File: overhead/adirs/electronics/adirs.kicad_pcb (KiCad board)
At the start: 2 copper layers, 3 parts

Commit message: Exported DSN and SES for ADIRS
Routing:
- net Net-(KR1-+5V_TOP_LED): track 0.00 -> 18.6 mm
- net Net-(KR1-GND_TOP_LED): track 0.06 -> 16.5 mm
- net Net-(KR1-+5V_BOTTOM_LED): track 0.00 -> 2.54 mm
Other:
- board outline added: 147.7 x 51.2 mm
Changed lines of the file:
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@@
 		(layer "Dwgs.User")
 	)
+	(gr_rect
+		(start 47.2 97.4)
+		(end 194.9 148.6)
+		(stroke
+			(width 0.05)
+			(type default)
+		)
+		(fill no)
+		(layer "Edge.Cuts")
+	)
 	(segment
-		(start 96.65 125.79)
-		(end 96.61 125.75)
+		(start 97.9617 123.79)
+		(end 96.0017 125.75)
 		(width 0.2)
 		(layer "F.Cu")
 		(net 1)
 	)
+	(segment
+		(start 94.95 125.75)
+		(end 96.0017 125.75)
+		(width 0.2)
+		(layer "F.Cu")
+		(net 1)
+	)
+	(segment
+		(start 110.65 123.79)
+		(end 97.9617 123.79)
+		(width 0.2)
+		(layer "F.Cu")
+		(net 1)
+	)
+	(segment
+		(start 110.65 126.33)
+		(end 110.65 128.87)
+		(width 0.2)
+		(layer "B.Cu")
+		(net 2)
+	)
+	(segment
+		(start 102.5583 128.29)
+		(end 109.5983 121.25)
+		(width 0.2)
+		(layer "B.Cu")
+		(net 3)
+	)
+	(segment
+		(start 110.65 121.25)
+		(end 109.5983 121.25)
+		(width 0.2)
+		(layer "B.Cu")
+		(net 3)
+	)
+	(segment
+		(start 94.95 128.29)
+		(end 102.5583 128.29)
+		(width 0.2)
+		(layer "B.Cu")
+		(net 3)
+	)
 	(embedded_fonts no)

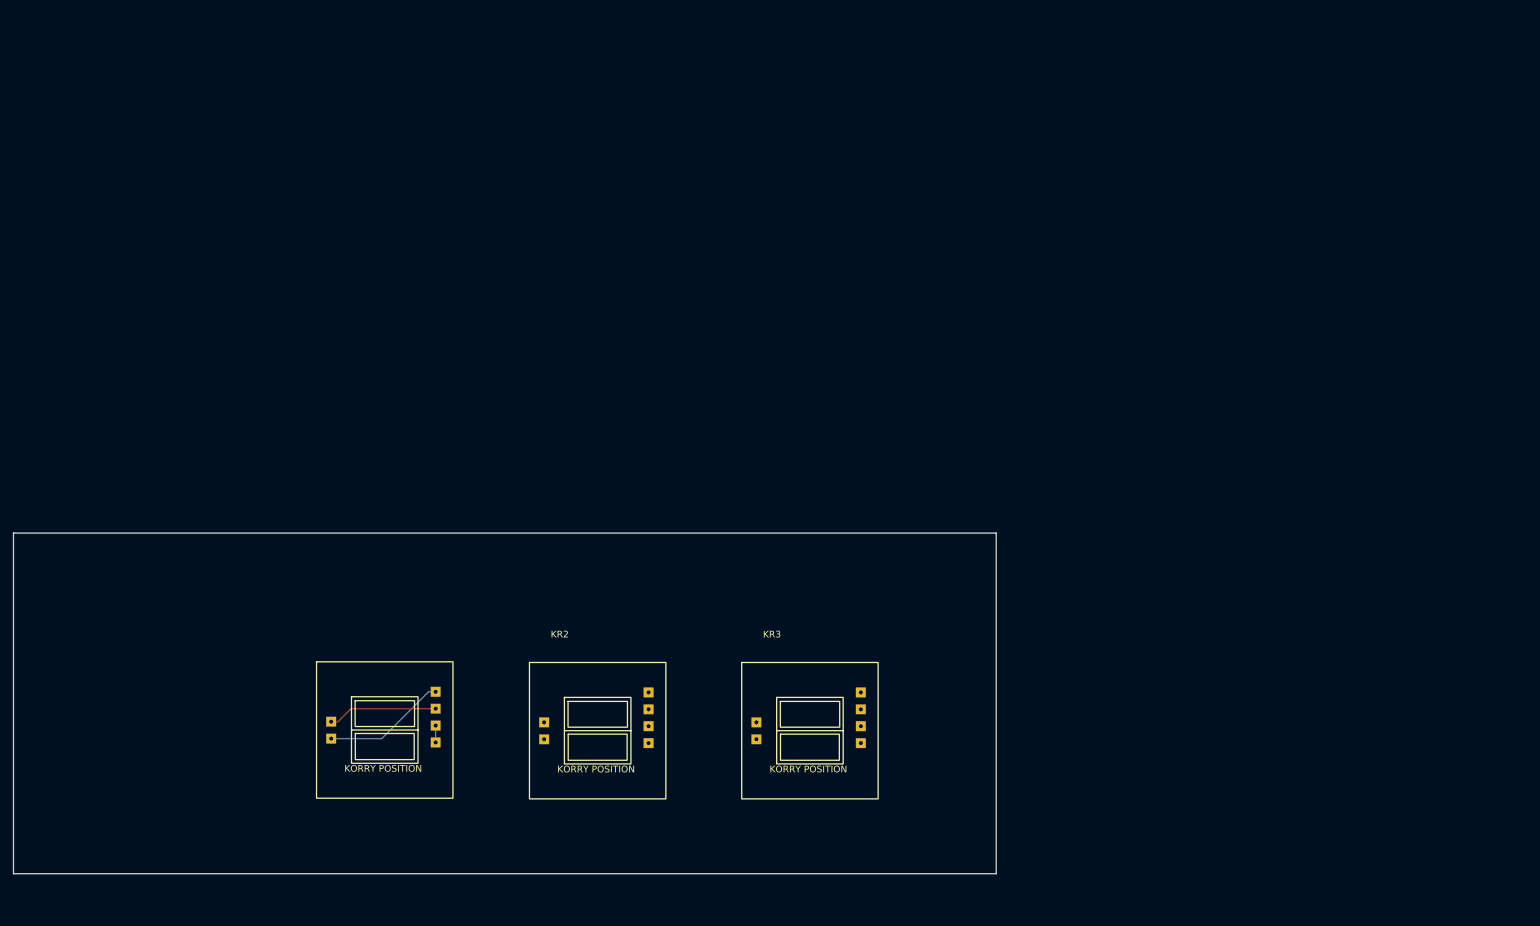
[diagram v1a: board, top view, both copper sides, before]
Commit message: Started work for ADIRS Schematic and PCB
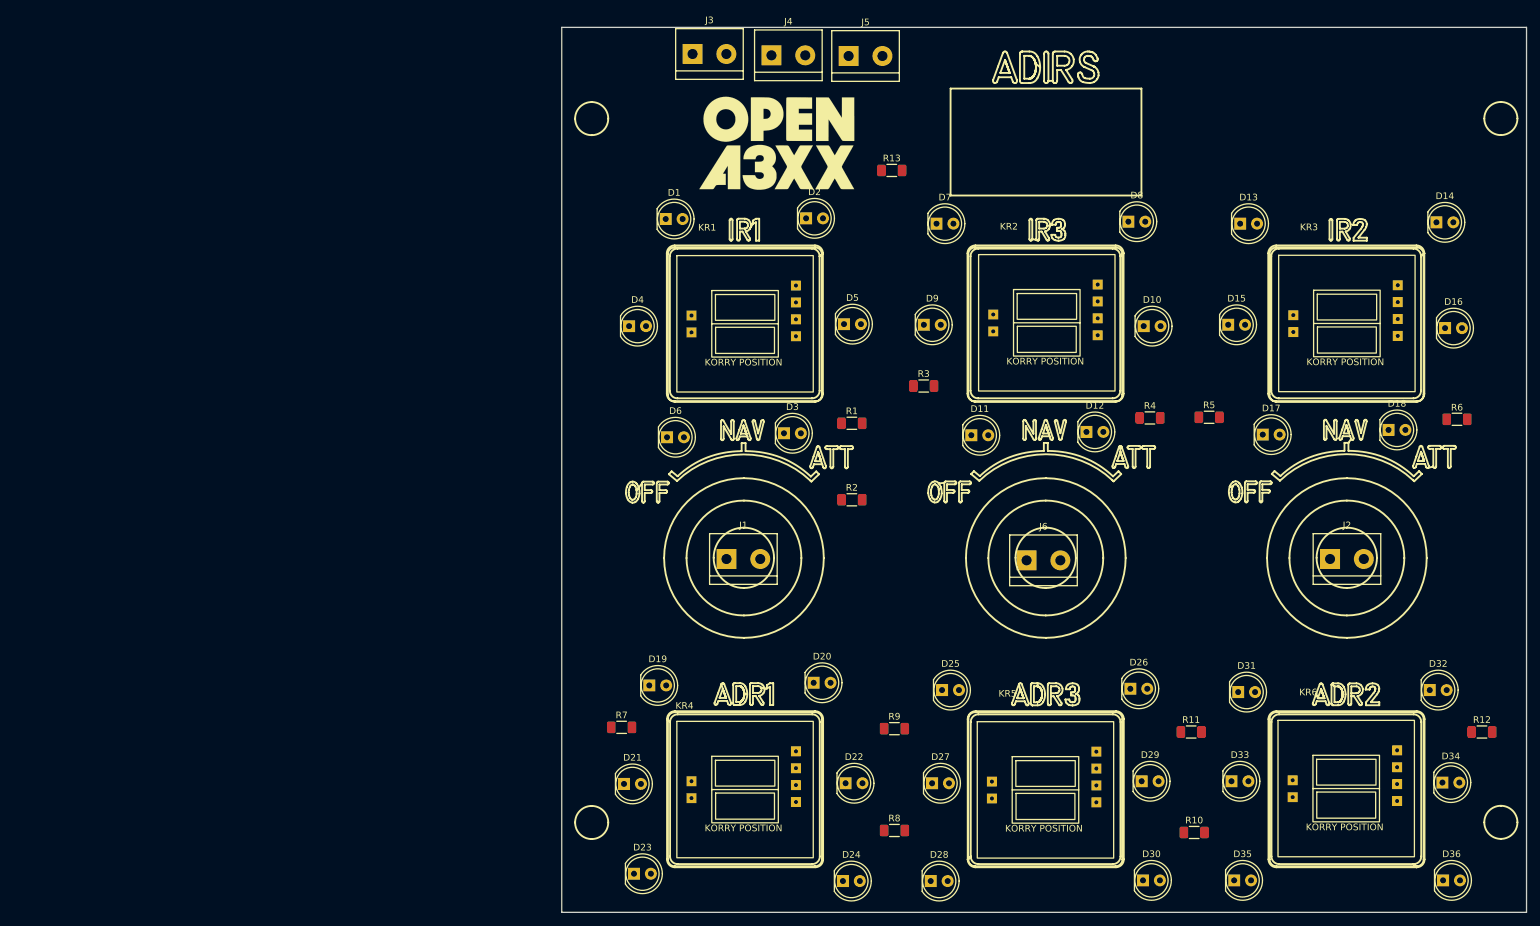
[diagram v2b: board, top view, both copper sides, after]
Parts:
- added D1: LED, LED_THT:LED_D5.0mm, F.Cu at (145.2, 50.2)
- added D10: LED, LED_THT:LED_D5.0mm, F.Cu at (217.1, 66.3)
- added D11: LED, LED_THT:LED_D5.0mm, F.Cu at (191.2, 82.7)
- added D12: LED, LED_THT:LED_D5.0mm, F.Cu at (208.5, 82.2)
- added D13: LED, LED_THT:LED_D5.0mm, F.Cu at (231.6, 50.9)
- added D14: LED, LED_THT:LED_D5.0mm, F.Cu at (261.1, 50.7)
- added D15: LED, LED_THT:LED_D5.0mm, F.Cu at (229.8, 66.1)
- added D16: LED, LED_THT:LED_D5.0mm, F.Cu at (262.4, 66.6)
- added D17: LED, LED_THT:LED_D5.0mm, F.Cu at (235.0, 82.6)
- added D18: LED, LED_THT:LED_D5.0mm, F.Cu at (253.9, 81.9)
- added D19: LED, LED_THT:LED_D5.0mm, F.Cu at (142.8, 120.3)
- added D2: LED, LED_THT:LED_D5.0mm, F.Cu at (166.3, 50.1)
- added D20: LED, LED_THT:LED_D5.0mm, F.Cu at (167.5, 119.9)
- added D21: LED, LED_THT:LED_D5.0mm, F.Cu at (139.0, 135.1)
- added D22: LED, LED_THT:LED_D5.0mm, F.Cu at (172.3, 135.0)
- added D23: LED, LED_THT:LED_D5.0mm, F.Cu at (140.5, 148.6)
- added D24: LED, LED_THT:LED_D5.0mm, F.Cu at (171.9, 149.7)
- added D25: LED, LED_THT:LED_D5.0mm, F.Cu at (186.8, 121.0)
- added D26: LED, LED_THT:LED_D5.0mm, F.Cu at (215.1, 120.8)
- added D27: LED, LED_THT:LED_D5.0mm, F.Cu at (185.3, 135.0)
- added D28: LED, LED_THT:LED_D5.0mm, F.Cu at (185.1, 149.7)
- added D29: LED, LED_THT:LED_D5.0mm, F.Cu at (216.8, 134.7)
- added D3: LED, LED_THT:LED_D5.0mm, F.Cu at (163.0, 82.4)
- added D30: LED, LED_THT:LED_D5.0mm, F.Cu at (217.0, 149.6)
- added D31: LED, LED_THT:LED_D5.0mm, F.Cu at (231.3, 121.3)
- added D32: LED, LED_THT:LED_D5.0mm, F.Cu at (260.1, 121.0)
- added D33: LED, LED_THT:LED_D5.0mm, F.Cu at (230.3, 134.7)
- added D34: LED, LED_THT:LED_D5.0mm, F.Cu at (262.0, 134.9)
- added D35: LED, LED_THT:LED_D5.0mm, F.Cu at (230.7, 149.6)
- added D36: LED, LED_THT:LED_D5.0mm, F.Cu at (262.1, 149.6)
- added D4: LED, LED_THT:LED_D5.0mm, F.Cu at (139.7, 66.3)
- added D5: LED, LED_THT:LED_D5.0mm, F.Cu at (172.0, 66.0)
- added D6: LED, LED_THT:LED_D5.0mm, F.Cu at (145.4, 83.0)
- added D7: LED, LED_THT:LED_D5.0mm, F.Cu at (185.9, 50.9)
- added D8: LED, LED_THT:LED_D5.0mm, F.Cu at (214.8, 50.6)
- added D9: LED, LED_THT:LED_D5.0mm, F.Cu at (184.0, 66.1)
- added G***: LOGO, opena3x:Logo, F.Cu at (161.5, 39.0)
- added J1: Conn_02x01, TerminalBlock:TerminalBlock_bornier-2_P5.08mm, F.Cu at (154.4, 101.3)
- added J2: Conn_02x13_Counter_Clockwise, TerminalBlock:TerminalBlock_bornier-2_P5.08mm, F.Cu at (245.1, 101.3)
- added J3: Conn_02x01, TerminalBlock:TerminalBlock_bornier-2_P5.08mm, F.Cu at (149.3, 25.4)
- added J4: Conn_02x02_Counter_Clockwise, TerminalBlock:TerminalBlock_bornier-2_P5.08mm, F.Cu at (161.1, 25.6)
- added J5: Conn_02x02_Counter_Clockwise, TerminalBlock:TerminalBlock_bornier-2_P5.08mm, F.Cu at (172.7, 25.7)
- added J6: Conn_02x02_Counter_Clockwise, TerminalBlock:TerminalBlock_bornier-2_P5.08mm, F.Cu at (199.5, 101.5)
- added KR4: ~, KorrySwitch:OpenA3XX, F.Cu at (146.9, 125.7)
- added KR5: ~, KorrySwitch:OpenA3XX, F.Cu at (192.1, 125.8)
- added KR6: ~, KorrySwitch:OpenA3XX, F.Cu at (237.2, 125.5)
- added R1: 220R, Resistor_SMD:R_1206_3216Metric_Pad1.30x1.75mm_HandSolder, F.Cu at (173.2, 80.9)
- added R10: 220R, Resistor_SMD:R_1206_3216Metric_Pad1.30x1.75mm_HandSolder, F.Cu at (224.7, 142.4)
- added R11: 220R, Resistor_SMD:R_1206_3216Metric_Pad1.30x1.75mm_HandSolder, F.Cu at (224.2, 127.3)
- added R12: 220R, Resistor_SMD:R_1206_3216Metric_Pad1.30x1.75mm_HandSolder, F.Cu at (267.9, 127.3)
- added R13: 220R, Resistor_SMD:R_1206_3216Metric_Pad1.30x1.75mm_HandSolder, F.Cu at (179.2, 42.9)
- added R2: 220R, Resistor_SMD:R_1206_3216Metric_Pad1.30x1.75mm_HandSolder, F.Cu at (173.2, 92.4)
- added R3: 220R, Resistor_SMD:R_1206_3216Metric_Pad1.30x1.75mm_HandSolder, F.Cu at (184.0, 75.3)
- added R4: 220R, Resistor_SMD:R_1206_3216Metric_Pad1.30x1.75mm_HandSolder, F.Cu at (218.0, 80.1)
- added R5: 220R, Resistor_SMD:R_1206_3216Metric_Pad1.30x1.75mm_HandSolder, F.Cu at (226.9, 80.0)
- added R6: 220R, Resistor_SMD:R_1206_3216Metric_Pad1.30x1.75mm_HandSolder, F.Cu at (264.1, 80.3)
- added R7: 220R, Resistor_SMD:R_1206_3216Metric_Pad1.30x1.75mm_HandSolder, F.Cu at (138.6, 126.6)
- added R8: 220R, Resistor_SMD:R_1206_3216Metric_Pad1.30x1.75mm_HandSolder, F.Cu at (179.6, 142.1)
- added R9: 220R, Resistor_SMD:R_1206_3216Metric_Pad1.30x1.75mm_HandSolder, F.Cu at (179.6, 126.8)
- moved KR3 101.3 mm to (237.3, 55.6)
- moved KR2 91.2 mm to (192.2, 55.5)
- moved KR1 81.6 mm to (146.9, 55.7)
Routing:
- net Net-(KR1-+5V_TOP_LED): track 18.6 -> 0.00 mm
- net Net-(KR1-GND_TOP_LED): track 16.5 -> 0.00 mm
- net Net-(KR1-+5V_BOTTOM_LED): track 2.54 -> 0.00 mm
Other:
- board size 147.7 x 51.2 mm -> 145 x 133 mm

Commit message: Updates and Routing to ADIRS PCB and Schematic
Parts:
- removed the G*** at (161.5, 39.0)
- added D37: LED, LED_THT:LED_D5.0mm, F.Cu at (188.4, 27.2)
- added D38: LED, LED_THT:LED_D5.0mm, F.Cu at (182.1, 37.8)
- added D39: LED, LED_THT:LED_D5.0mm, F.Cu at (213.3, 27.4)
- added D40: LED, LED_THT:LED_D5.0mm, F.Cu at (218.4, 39.1)
- added G***: LOGO, opena3x:Logo, F.Cu at (162.4, 39.8)
- added G***: LOGO, opena3x:Logo, B.Cu at (164.3, 39.2)
- added R14: 220R, Resistor_SMD:R_1206_3216Metric_Pad1.30x1.75mm_HandSolder, F.Cu at (224.6, 30.6)
- added R15: 220R, Resistor_SMD:R_1206_3216Metric_Pad1.30x1.75mm_HandSolder, F.Cu at (228.6, 39.3)
- J2: footprint TerminalBlock:TerminalBlock_bornier-2_P5.08mm -> Connector_PinHeader_2.54mm:PinHeader_2x14_P2.54mm_Vertical; moved to B.Cu
- J3: footprint TerminalBlock:TerminalBlock_bornier-2_P5.08mm -> Connector_PinHeader_2.54mm:PinHeader_1x02_P2.54mm_Vertical
- J4, J5, J6: footprint TerminalBlock:TerminalBlock_bornier-2_P5.08mm -> TerminalBlock:TerminalBlock_bornier-4_P5.08mm
- moved J5 111.8 mm to (255.2, 101.2), turned to 180 degrees
- moved J2 76.5 mm to (235.1, 25.5), turned to -90 degrees
- moved J1 76.0 mm to (154.2, 25.3), turned to 180 degrees
- moved J4 75.6 mm to (164.6, 101.1), turned to 180 degrees
- moved J3 56.7 mm to (204.4, 38.5), turned to -90 degrees
- moved J6 10.4 mm to (209.9, 101.1), turned to 180 degrees
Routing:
- net GND: track 0.00 -> 680.1 mm, vias 0 -> 4
- net +12V: track 0.00 -> 470.3 mm, vias 0 -> 3
- net Net-(J2-Pin_15): track 0.00 -> 208.4 mm, vias 0 -> 1
- net Net-(J2-Pin_14): track 0.00 -> 191.0 mm, vias 0 -> 1
- net Net-(J2-Pin_13): track 0.00 -> 185.4 mm, vias 0 -> 1
- net Net-(J2-Pin_21): track 0.00 -> 178.1 mm, vias 0 -> 1
- net Net-(J2-Pin_22): track 0.00 -> 177.3 mm, vias 0 -> 1
- net Net-(J2-Pin_20): track 0.00 -> 161.9 mm, vias 0 -> 2
- net Net-(J2-Pin_9): track 0.00 -> 146.7 mm, vias 0 -> 1
- net Net-(J2-Pin_28): track 0.00 -> 145.5 mm, vias 0 -> 1
- net Net-(J2-Pin_27): track 0.00 -> 143.3 mm, vias 0 -> 1
- net Net-(J2-Pin_7): track 0.00 -> 133.6 mm, vias 0 -> 2
- net Net-(J2-Pin_26): track 0.00 -> 132.6 mm, vias 0 -> 1
- net Net-(J2-Pin_3): track 0.00 -> 128.6 mm, vias 0 -> 1
- net Net-(J2-Pin_8): track 0.00 -> 125.0 mm, vias 0 -> 1
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
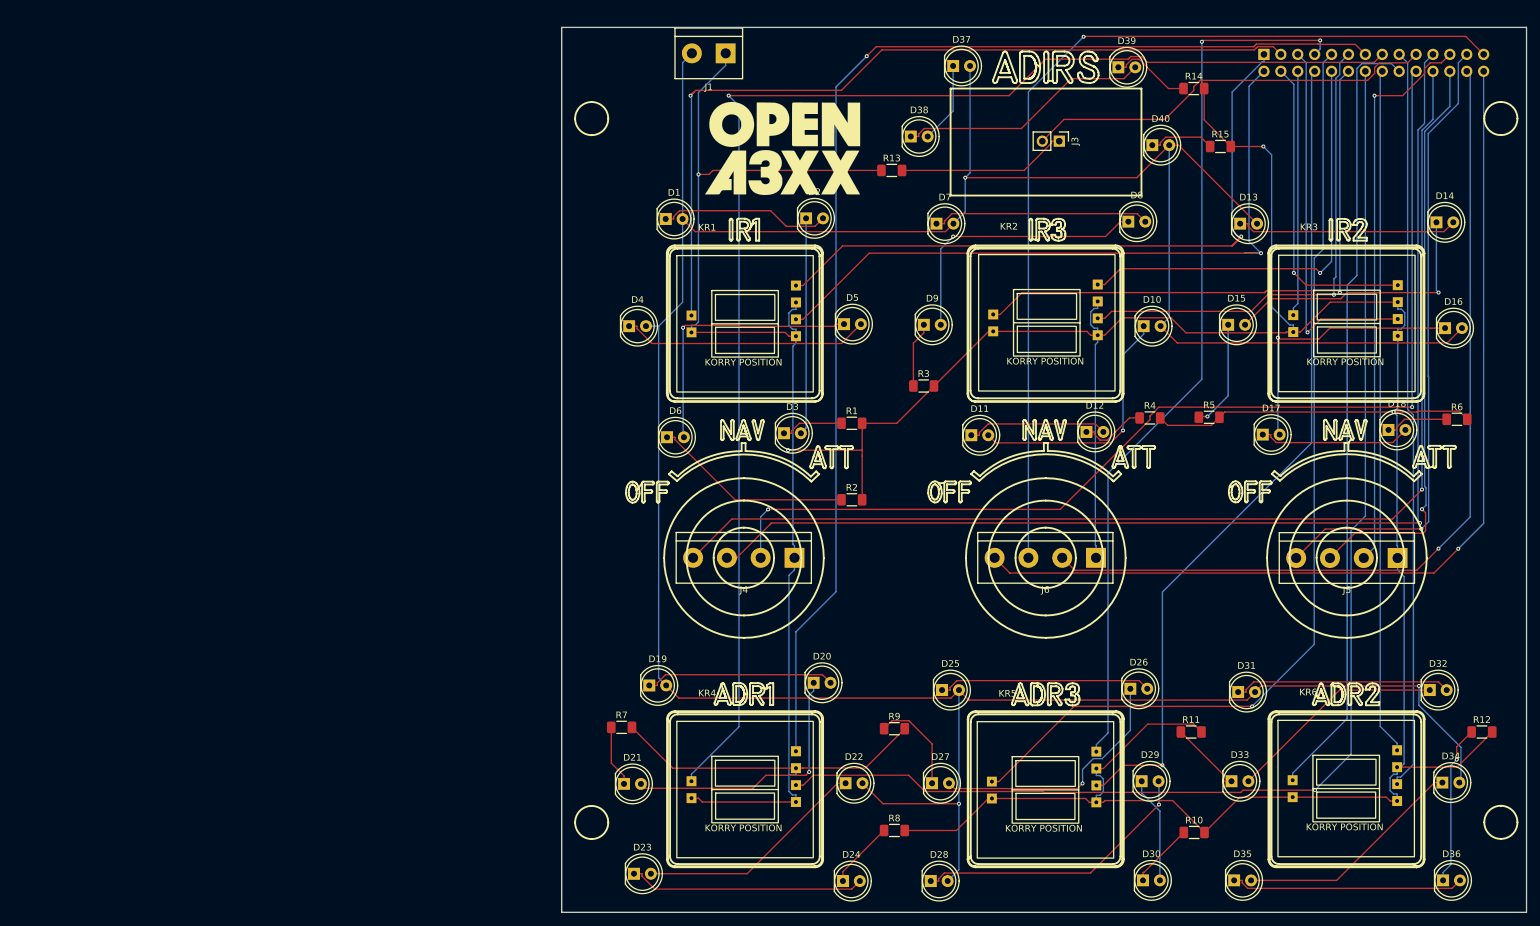
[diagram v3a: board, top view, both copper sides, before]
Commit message: Improvements to ADIRS - and setting up PCB design Baseline
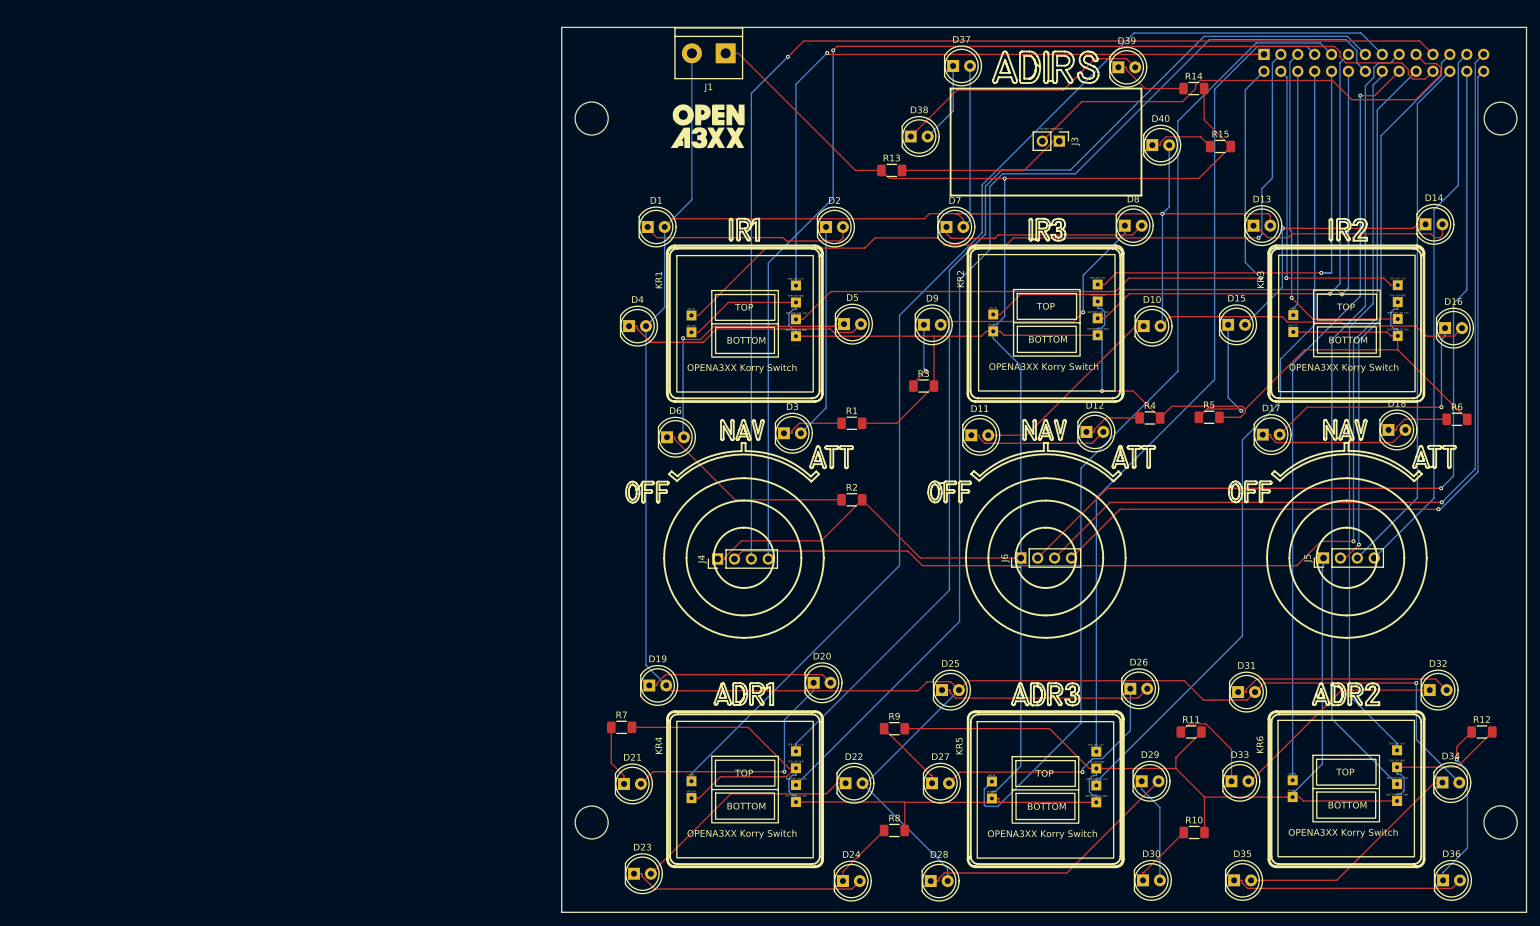
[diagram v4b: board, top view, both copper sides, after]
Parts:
- removed the G*** at (162.4, 39.8)
- removed the G*** at (164.3, 39.2)
- added G***: LOGO, OpenA3XX:OpenA3XXLogoSmall, F.Cu at (151.6, 36.2)
- added G***: LOGO, OpenA3XX:OpenA3XXLogoSmall, B.Cu at (151.6, 36.2)
- D1, D10, D11, D12, D13, D14, D15, D16, D17, D18, D19, D2, D20, D21, D22, D23, D24, D25, D26, D27, D28, D29, D3, D30, D31, D32, D33, D34, D35, D36, D37, D38, D39, D4, D40, D5, D6, D7, D8, D9: footprint LED_THT:LED_D5.0mm -> LED_THT:LED_D5.0mm_Clear
- J4, J5, J6: footprint TerminalBlock:TerminalBlock_bornier-4_P5.08mm -> Connector_PinHeader_2.54mm:PinHeader_1x04_P2.54mm_Vertical
- KR1, KR2, KR3, KR4, KR5, KR6: footprint KorrySwitch:OpenA3XX -> OpenA3XX:Korry Switch
- moved J4 11.6 mm to (153.0, 101.3), turned to 90 degrees
- moved J6 11.3 mm to (198.6, 101.2), turned to 90 degrees
- moved J5 11.1 mm to (244.1, 101.2), turned to 90 degrees
- moved D2 3.27 mm to (169.3, 51.4)
- moved D1 2.95 mm to (142.5, 51.4)
- moved D13 2.02 mm to (233.6, 51.2)
- moved D14 1.66 mm to (259.4, 51.0)
- moved D7 1.58 mm to (187.4, 51.4)
- moved D8 0.80 mm to (214.2, 51.2)
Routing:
- net Net-(J2-Pin_15): track 208.4 -> 178.6 mm, vias 1 -> 0
- net GND: track 680.1 -> 708.8 mm, vias 4 -> 2
- net Net-(J2-Pin_13): track 185.4 -> 164.3 mm, vias 1 -> 0
- net Net-(J2-Pin_14): track 191.0 -> 170.6 mm, vias 1 -> 0
- net Net-(J2-Pin_28): track 145.5 -> 127.0 mm
- net Net-(J2-Pin_25): track 94.8 -> 81.5 mm, vias 1 -> 0
- net Net-(J2-Pin_27): track 143.3 -> 131.6 mm
- net Net-(J2-Pin_19): track 62.4 -> 72.3 mm
- net Net-(J2-Pin_3): track 128.6 -> 119.9 mm
- net Net-(J2-Pin_20): track 161.9 -> 170.5 mm, vias 2 -> 1
- net Net-(J2-Pin_7): track 133.6 -> 125.1 mm, vias 2 -> 0
- net Net-(J2-Pin_24): track 87.2 -> 78.9 mm, vias 1 -> 0
- net Net-(D10-K): track 38.5 -> 30.2 mm, vias 1 -> 0
- net Net-(J2-Pin_17): track 111.9 -> 119.0 mm
- net Net-(D1-K): track 25.8 -> 32.2 mm
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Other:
- outline, holes or cut-outs redrawn
- board text added: "+12V Variable Backlight"
- board text added: "GND"
- board text added: "ON_BAT INDICATOR"
